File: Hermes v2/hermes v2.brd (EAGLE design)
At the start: 25.4 x 50.8 mm, 28 parts, among them IC1 LM3914V, K1 LCC110STR, Q1 BSS123, Q2 BSS84, U1 DAC, U2 AD8067

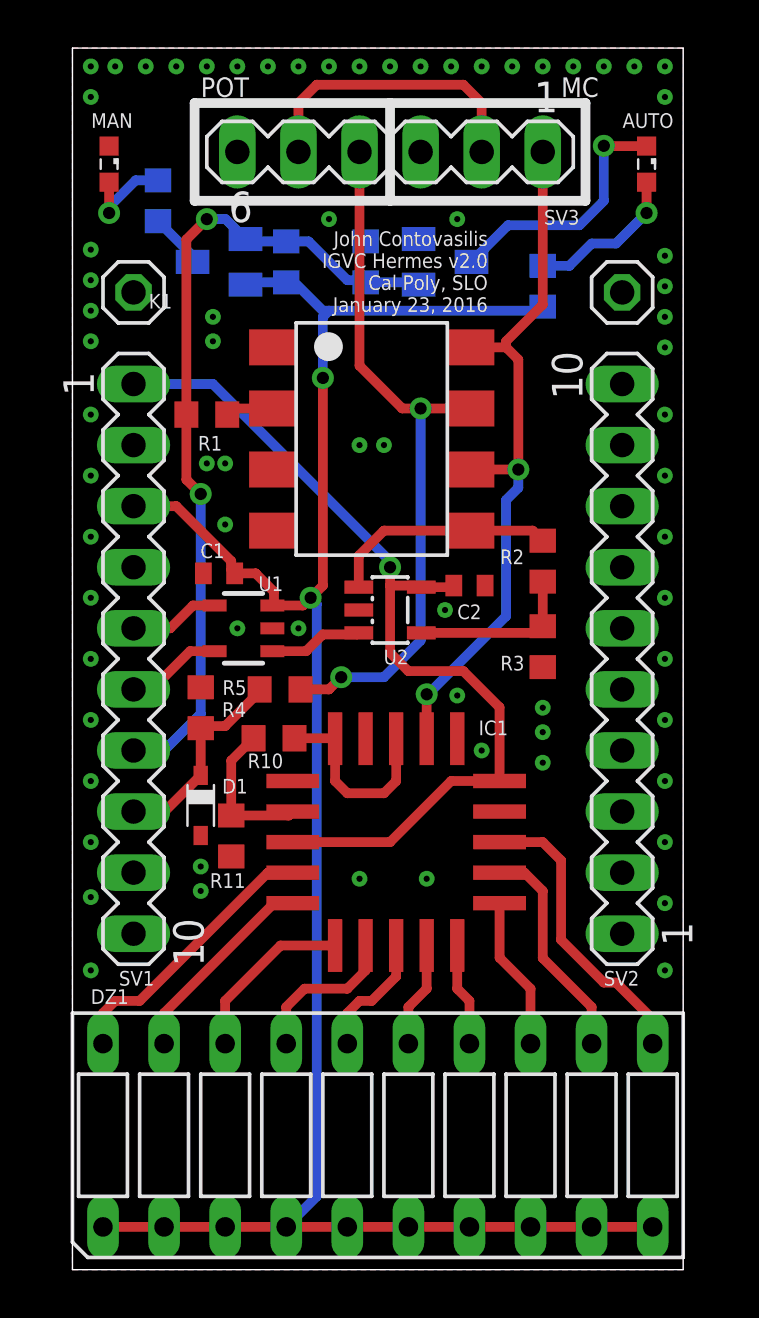
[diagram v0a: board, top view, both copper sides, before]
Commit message: fixed hermes issues
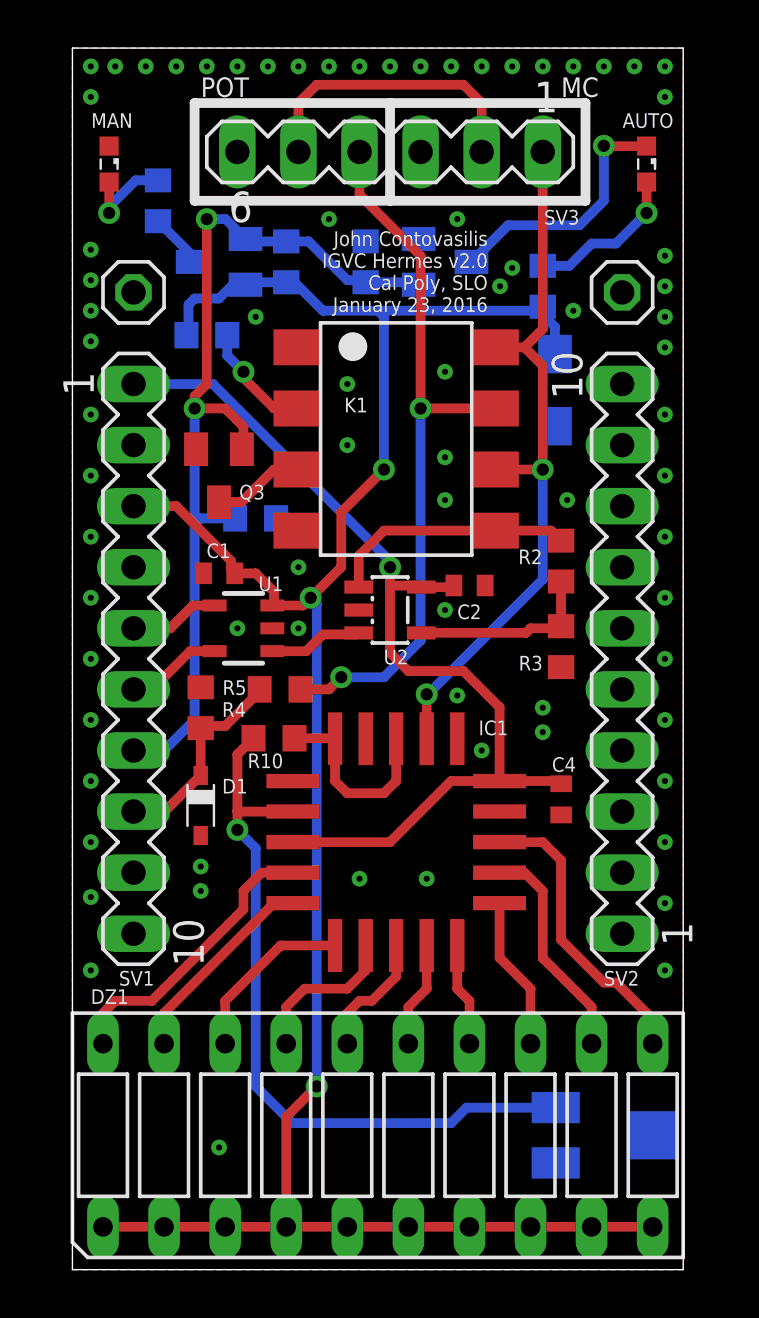
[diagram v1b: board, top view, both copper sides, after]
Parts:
- added C3: 2.2uF, rcl:SMC_A
- added C4: .1uF, eagle-ltspice:C0402
- added Q3: BSS123, transistor-small-signal:SOT23
- added R12: 10K, resistor:R0603
- R11: device resistor:R0603 -> rcl:RTRIM5X
- moved R11 19.9 mm to (20.8, 5.59), flipped to the bottom, turned to 90 degrees
- moved R1 3.30 mm to (4.32, 38.9), flipped to the bottom
- moved K1 1.02 mm to (12.2, 34.5)
- moved R2 0.76 mm to (19.1, 29.5)
- moved R3 0.76 mm to (19.1, 25.9)
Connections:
- new net CONTROL_-: K1.3, Q3.3
- net CONTROL_+: now also R1.2; no longer R1.1
- net ENABLE: now also Q3.1, R12.1; no longer R1.2
- net GND: now also C3.-, C4.2, Q3.2, R11.1, R12.2; no longer K1.3
- net N$15: now also R11.3; no longer R11.1
- net PP12V: now also C4.1
- net PP3V3: now also C3.+, R1.1
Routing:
- net N$15: track 6.23 -> 30.8 mm, vias 0 -> 1
- net PP3V3: track 84.7 -> 91.9 mm, vias 2 -> 3
- net ENABLE: track 34.5 -> 39.1 mm
- net CONTROL_-: track 0.00 -> 3.78 mm
- net CONTROL_+: track 1.96 -> 4.78 mm, vias 0 -> 1
- net PP12V: track 38.4 -> 41.1 mm
- net OP_AMP_OUT: track 9.56 -> 10.3 mm
- net NON-INVERT: track 7.02 -> 7.78 mm
- net ACC_POT_W: track 29.8 -> 30.3 mm

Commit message: fixed more hermes things
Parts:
- removed SV3: (no value), con-lstb:MA06-1
- added R13: 0, rcl:R0402
- added X1: (no value), con-molex:22-23-2061
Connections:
- removed net THROTTLE_+: SV3.2, SV3.5
- new net THROTTLE_+M: R13.1, X1.5
- new net THROTTLE_+P: R13.2, X1.2
- net ACC_POT_W: now also X1.3; no longer SV3.4
- net GND: now also X1.1, X1.4; no longer SV3.3, SV3.6
- net THROTTLE_S: now also X1.6; no longer SV3.1
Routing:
- net THROTTLE_+: track 12.3 -> 0.00 mm
- net THROTTLE_+P: track 0.00 -> 5.25 mm
- net THROTTLE_+M: track 0.00 -> 5.10 mm
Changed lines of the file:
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@@
 Cal Poly, SLO
 January 23, 2016</text>
-<wire x1="3.81" y1="48.514" x2="11.938" y2="48.514" width="0.4064" layer="21"/>
-<wire x1="11.938" y1="48.514" x2="20.066" y2="48.514" width="0.4064" layer="21"/>
-<wire x1="20.066" y1="48.514" x2="20.066" y2="44.45" width="0.4064" layer="21"/>
-<wire x1="20.066" y1="44.45" x2="11.938" y2="44.45" width="0.4064" layer="21"/>
-<wire x1="11.938" y1="44.45" x2="3.81" y2="44.45" width="0.4064" layer="21"/>
-<wire x1="3.81" y1="44.45" x2="3.81" y2="48.514" width="0.4064" layer="21"/>
-<wire x1="11.938" y1="48.514" x2="11.938" y2="44.45" width="0.4064" layer="21"/>
-<text x="4.064" y="48.768" size="0.8128" layer="21" font="vector" ratio="15">POT</text>
-<text x="19.05" y="48.768" size="0.8128" layer="21" font="vector" ratio="15">MC</text>
+<text x="3.81" y="45.212" size="0.8128" layer="21" font="vector" ratio="15" rot="R90">POT</text>
+<text x="20.828" y="44.958" size="0.8128" layer="21" font="vector" ratio="15" rot="R90">MC</text>
 </plain>
 <attributes>
@@
 <attribute name="VALUE" x="0" y="37.465" size="1.27" layer="27"/>
 </element>
-<element name="SV3" library="con-lstb" package="MA06-1" value="" x="11.938" y="46.482" smashed="yes" rot="R180">
-<attribute name="MF" value="" x="11.938" y="46.482" size="1.778" layer="27" rot="R180" display="off"/>
-<attribute name="OC_FARNELL" value="unknown" x="11.938" y="46.482" size="1.778" layer="27" rot="R180" display="off"/>
-<attribute name="OC_NEWARK" value="unknown" x="11.938" y="46.482" size="1.778" layer="27" rot="R180" display="off"/>
-<attribute name="MPN" value="" x="11.938" y="46.482" size="1.778" layer="27" rot="R180" display="off"/>
-<attribute name="NAME" x="19.812" y="44.069" size="0.6096" layer="25" font="vector" ratio="15" rot="R180"/>
-<attribute name="VALUE" x="14.478" y="49.403" size="1.27" layer="27" ratio="10" rot="R180"/>
-</element>
 <element name="K1" library="relay" package="DIL08SMD" value="LCC110STR" x="12.192" y="34.544" smashed="yes" rot="R270">
 <attribute name="MF" value="AROMAT/ MATSUSHITA" x="12.192" y="34.544" size="1.778" layer="27" rot="R270" display="off"/>
@@
 <attribute name="VALUE" x="18.288" y="10.033" size="1.27" layer="28" rot="MR180"/>
 <attribute name="DIGI" value="490-2678-1-ND" x="20.828" y="5.588" size="1.778" layer="28" rot="MR90" display="off"/>
+</element>
+<element name="X1" library="con-molex" package="22-23-2061" value="" x="11.938" y="46.482" smashed="yes">
+<attribute name="MF" value="MOLEX" x="11.938" y="46.482" size="1.778" layer="27" display="off"/>
+<attribute name="OC_NEWARK" value="27C1933" x="11.938" y="46.482" size="1.778" layer="27" display="off"/>
+<attribute name="OC_FARNELL" value="1462922" x="11.938" y="46.482" size="1.778" layer="27" display="off"/>
+<attribute name="MPN" value="22-23-2061" x="11.938" y="46.482" size="1.778" layer="27" display="off"/>
+<attribute name="NAME" x="3.048" y="48.768" size="0.6096" layer="25" font="vector" ratio="15"/>
+<attribute name="VALUE" x="4.318" y="41.402" size="1.016" layer="27" ratio="10"/>
+</element>
+<element name="R13" library="rcl" package="R0402" value="0" x="11.938" y="49.022" smashed="yes" rot="MR0">
+<attribute name="NAME" x="14.859" y="48.641" size="0.6096" layer="26" font="vector" ratio="15" rot="MR0"/>
+<attribute name="VALUE" x="12.573" y="47.117" size="1.27" layer="28" rot="MR0"/>
 </element>
 </elements>
@@
 </polygon>
 <contactref element="R5" pad="2"/>
-<contactref element="SV3" pad="6"/>
-<contactref element="SV3" pad="3"/>
 <contactref element="D1" pad="A"/>
 <contactref element="Q1" pad="2"/>
@@
 <via x="19.304" y="32.004" extent="1-16" drill="0.254"/>
 <via x="4.826" y="5.08" extent="1-16" drill="0.254"/>
+<contactref element="X1" pad="4"/>
+<contactref element="X1" pad="1"/>
 </signal>
 <signal name="I2C_SDA">
@@
 </signal>
 <signal name="ACC_POT_W">
-<contactref element="SV3" pad="4"/>
 <contactref element="K1" pad="7"/>
 <contactref element="R4" pad="1"/>
@@
 <wire x1="13.208" y1="35.814" x2="16.342" y2="35.814" width="0.4064" layer="1"/>
 <wire x1="8.216" y1="24.13" x2="9.398" y2="24.13" width="0.4064" layer="1"/>
-<wire x1="10.668" y1="46.482" x2="10.668" y2="44.704" width="0.4064" layer="1"/>
 <wire x1="10.668" y1="44.704" x2="13.208" y2="42.164" width="0.4064" layer="1"/>
 <wire x1="13.208" y1="42.164" x2="13.208" y2="35.814" width="0.4064" layer="1"/>
-</signal>
-<signal name="THROTTLE_+">
-<contactref element="SV3" pad="5"/>
-<contactref element="SV3" pad="2"/>
-<wire x1="8.128" y1="46.482" x2="8.128" y2="48.514" width="0.4064" layer="1"/>
-<wire x1="8.128" y1="48.514" x2="8.89" y2="49.276" width="0.4064" layer="1"/>
-<wire x1="8.89" y1="49.276" x2="14.986" y2="49.276" width="0.4064" layer="1"/>
-<wire x1="14.986" y1="49.276" x2="15.748" y2="48.514" width="0.4064" layer="1"/>
-<wire x1="15.748" y1="48.514" x2="15.748" y2="46.482" width="0.4064" layer="1"/>
+<contactref element="X1" pad="3"/>
+<wire x1="10.668" y1="44.704" x2="10.668" y2="46.482" width="0.4064" layer="1"/>
+</signal>
+<signal name="THROTTLE_+P">
+<contactref element="X1" pad="2"/>
+<contactref element="R13" pad="2"/>
+<wire x1="8.128" y1="46.482" x2="8.128" y2="48.26" width="0.4064" layer="16"/>
+<wire x1="8.128" y1="48.26" x2="8.89" y2="49.022" width="0.4064" layer="16"/>
+<wire x1="8.89" y1="49.022" x2="11.288" y2="49.022" width="0.4064" layer="16"/>
 </signal>
 <signal name="THROTTLE_S">
-<contactref element="SV3" pad="1"/>
 <contactref element="K1" pad="6"/>
 <contactref element="K1" pad="8"/>
@@
 <wire x1="18.288" y1="28.702" x2="18.288" y2="33.274" width="0.4064" layer="16"/>
 <via x="18.288" y="33.274" extent="1-16" drill="0.508"/>
-<wire x1="18.288" y1="46.482" x2="18.288" y2="39.116" width="0.4064" layer="1"/>
 <wire x1="18.288" y1="28.702" x2="13.5128" y2="23.9268" width="0.4064" layer="16"/>
 <wire x1="13.5128" y1="23.9268" x2="13.462" y2="23.9268" width="0.4064" layer="16"/>
@@
 <wire x1="17.526" y1="38.354" x2="16.342" y2="38.354" width="0.4064" layer="1"/>
 <wire x1="18.288" y1="39.116" x2="17.526" y2="38.354" width="0.4064" layer="1"/>
+<contactref element="X1" pad="6"/>
+<wire x1="18.288" y1="39.116" x2="18.288" y2="46.482" width="0.4064" layer="1"/>
 </signal>
 <signal name="TH_ADC">
@@
 <wire x1="7.112" y1="33.274" x2="8.042" y2="33.274" width="0.4064" layer="1"/>
 </signal>
+<signal name="THROTTLE_+M">
+<contactref element="X1" pad="5"/>
+<contactref element="R13" pad="1"/>
+<wire x1="12.588" y1="49.022" x2="14.732" y2="49.022" width="0.4064" layer="16"/>
+<wire x1="14.732" y1="49.022" x2="15.748" y2="48.006" width="0.4064" layer="16"/>
+<wire x1="15.748" y1="48.006" x2="15.748" y2="46.482" width="0.4064" layer="16"/>
+</signal>
 </signals>
